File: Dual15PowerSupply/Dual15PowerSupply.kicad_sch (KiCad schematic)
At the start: 40 parts, among them J1 120VAC, J2 +/-15VDC, U1 LT3091xT7, U2 LT3081

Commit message: Design rules for creepage
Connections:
- net Vin-: now reaches C4.2, R1.1, R3.1, U1.3 (~{SHDN}), U1.4 (IN)
- net Vin+: now reaches C3.1, R2.2, U2.6 (IN)
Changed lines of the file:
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@@
+		)
+	)
+	(label "Vin+"
+		(at 140.97 30.48 0)
+		(effects
+			(font
+				(size 1.27 1.27)
+			)
+			(justify left bottom)
 		)
 	)
@@
 		(effects
 			(font
+				(size 1.27 1.27)
+			)
+			(justify left bottom)
+		)
+	)
+	(label "Vin-"
+		(at 140.97 86.36 0)
+		(effects
+			(font

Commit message: Layout in work
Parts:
- U1: value LT3091xT7 -> LT3091
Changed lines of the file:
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@@
 			)
 		)
-		(property "Value" "LT3091xT7"
+		(property "Value" "LT3091"
 			(at 173.99 93.98 0)
 			(show_name no)

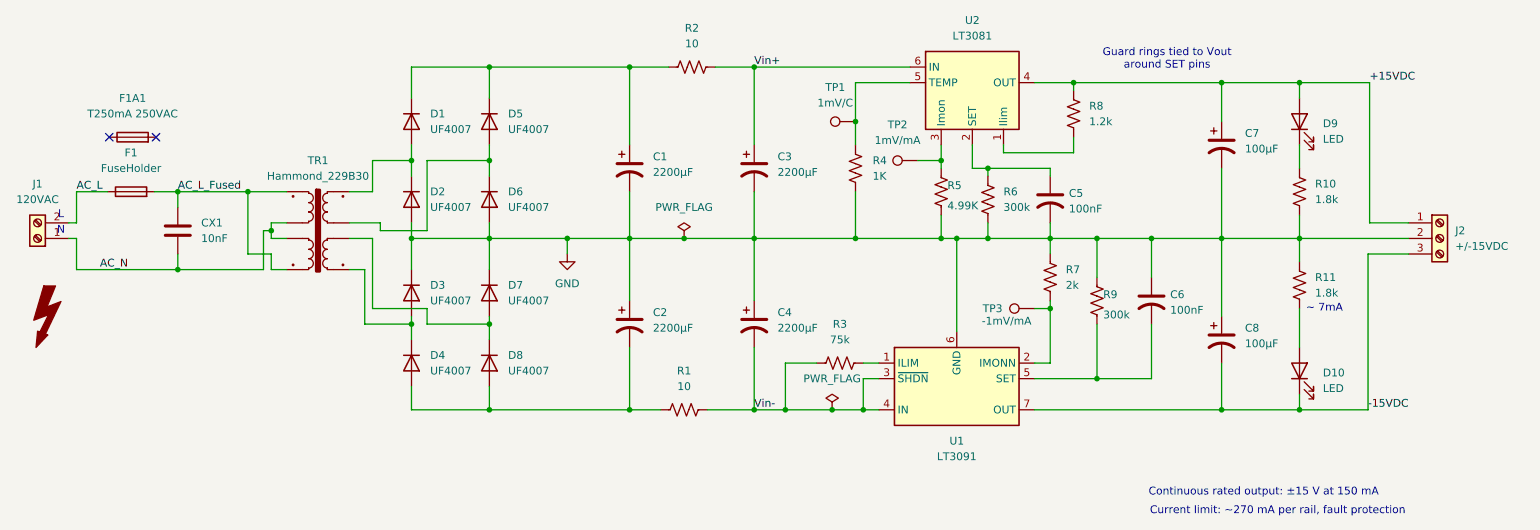
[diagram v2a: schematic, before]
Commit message: Change to SMD bridge rectifiers
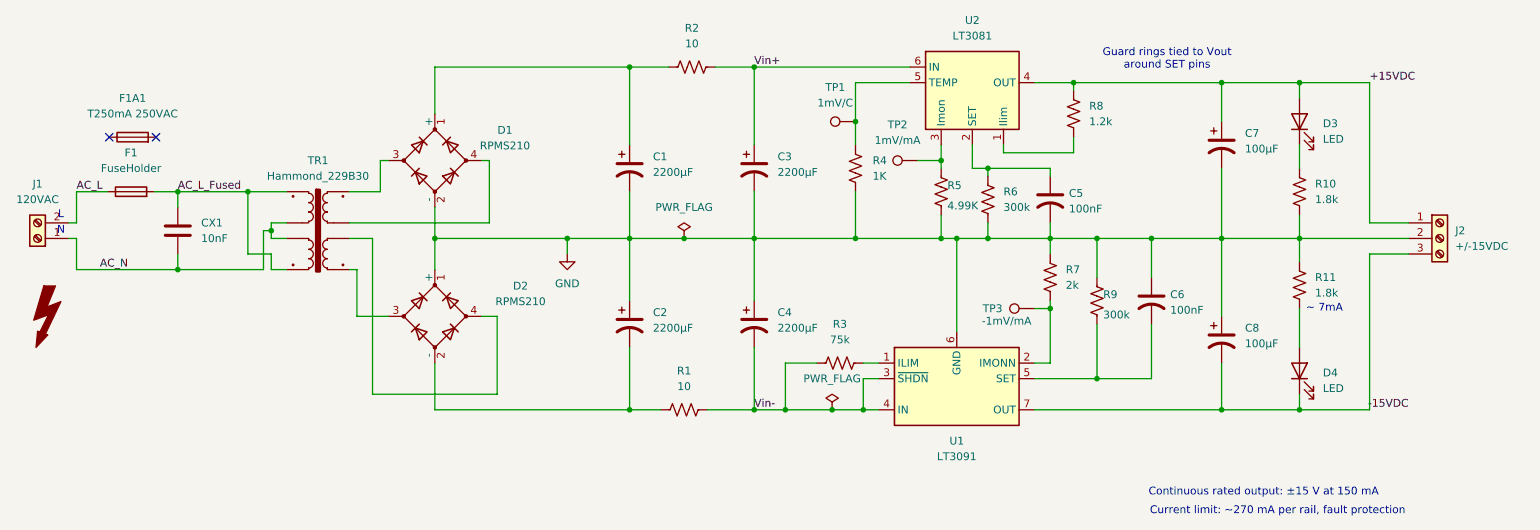
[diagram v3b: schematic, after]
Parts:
- removed D1, D2, D3, D4, D5, D6, D7, D8: UF4007, Diode_THT:D_DO-41_SOD81_P10.16mm_Horizontal, symbol Device:D
- added D1, D2: RPMS210, Diode_SMD_Bridge:Diode_Bridge_Panjit_M4_RPMS210, symbol Device:D_Bridge_+-AA
- R10, R11: footprint Resistor_THT:R_Axial_DIN0207_L6.3mm_D2.5mm_P15.24mm_Horizontal -> Resistor_SMD:R_1206_3216Metric_Pad1.30x1.75mm_HandSolder; MPN MF1/4LCT52R182J -> RT1206FRE071K8L; Mouser 660-MF1/4LCT52R182J -> 603-RT1206FRE071K8L
- TP1, TP2, TP3: MPN (none) -> 5005; Mouser (none) -> 534-5005
- renumbered D9 to D3, D10 to D4
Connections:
- net GND: now also D1.2 (-), D2.1 (+)
- net at C1.1, R2.1: now also D1.1 (+)
- net at TR1.8: now also D1.4
- net at TR1.7: now also D1.3
- net at TR1.5: now also D2.3
- net at TR1.6: now also D2.4
- net at C2.2, R1.2: now also D2.2 (-)

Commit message: Layout in progress
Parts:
- C1, C2: value 2200µF -> 1000µF; footprint Capacitor_THT:CP_Radial_D16.0mm_P7.50mm -> Capacitor_THT:CP_Radial_D12.5mm_P5.00mm; MPN UPW1V222MHD -> EEU-FR1V102; Mouser 647-UPW1V222MHD -> 667-EEU-FR1V102
- C3, C4: footprint Capacitor_THT:CP_Radial_D16.0mm_P7.50mm -> Capacitor_THT:CP_Radial_D12.5mm_P5.00mm; MPN UPW1V222MHD -> EEU-FR1V222L; Mouser 647-UPW1V222MHD -> 667-EEU-FR1V222L
- F1: footprint Fuseholder_Wurth:Wurth_WR-FSH_696105003002 -> Fuseholder_Wurth_WR-FSH:J_Wurth_WR-FSH_696105003002
- J1: footprint TerminalBlock_762:MKDS 5_2-7,62 -> TerminalBlock_Phoenix:PHOENIX_1731721; MPN 1717729 -> 1731721; Mouser 651-1717729 -> 651-1731721
- U1: Mouser 584-LT3091ET7#PBF -> 584-LT3091ET7#PBF
- U2: footprint Package_TO_SOT_THT:TO-220-7_P2.54x5.08mm_StaggerOdd_Lead3.08mm_Vertical -> Package_TO_SOT_THT:TO-220-7_P2.54x3.7mm_StaggerOdd_Lead3.8mm_Vertical
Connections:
- net +15VDC: now also J2.3 (Pin_3); no longer J2.1 (Pin_1)
- net -15VDC: now also J2.1 (Pin_1); no longer J2.3 (Pin_3)
- net AC_L: now also J1.1 (Pin_1); no longer J1.2 (Pin_2)
- net AC_N: now also J1.2 (Pin_2); no longer J1.1 (Pin_1)
- net S4: now reaches D2.3, TR1.5
- net S3: now reaches D2.4, TR1.6
- net S1: now reaches D1.3, TR1.7
- net S2: now reaches D1.4, TR1.8
- net RawDC-: now reaches C2.2, D2.2 (-), R1.2
- net RawDC+: now reaches C1.1, D1.1 (+), R2.1
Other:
- moved on the sheet: J1

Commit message: layout
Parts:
- R4: footprint Resistor_SMD:R_1206_3216Metric_Pad1.30x1.75mm_HandSolder -> Resistor_SMD:R_0805_2012Metric_Pad1.20x1.40mm_HandSolder; MPN RC1206FR-101KL -> RT0805FRE071KL; Mouser 603-RC1206FR-101KL -> 603-RT0805FRE071KL
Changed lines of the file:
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@@
 			)
 		)
-		(property "Footprint" "Resistor_SMD:R_1206_3216Metric_Pad1.30x1.75mm_HandSolder"
+		(property "Footprint" "Resistor_SMD:R_0805_2012Metric_Pad1.20x1.40mm_HandSolder"
 			(at 158.496 47.244 90)
 			(hide yes)
@@
 			)
 		)
-		(property "MPN" "RC1206FR-101KL "
+		(property "MPN" "RT0805FRE071KL"
 			(at 157.48 46.99 0)
 			(hide yes)
@@
 			)
 		)
-		(property "Mouser" "603-RC1206FR-101KL "
+		(property "Mouser" "603-RT0805FRE071KL "
 			(at 157.48 46.99 0)
 			(hide yes)

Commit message: in work
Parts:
- R5: footprint Resistor_SMD:R_1206_3216Metric_Pad1.30x1.75mm_HandSolder -> Resistor_SMD:R_0805_2012Metric_Pad1.20x1.40mm_HandSolder; MPN RC1206FR-074K99L -> RT0805FRD074K99L; Mouser 603-RC1206FR-074K99L -> 603-RT0805FRD074K99L
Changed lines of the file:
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@@
 			)
 		)
-		(property "Footprint" "Resistor_SMD:R_1206_3216Metric_Pad1.30x1.75mm_HandSolder"
+		(property "Footprint" "Resistor_SMD:R_0805_2012Metric_Pad1.20x1.40mm_HandSolder"
 			(at 172.466 51.054 90)
 			(hide yes)
@@
 			)
 		)
-		(property "Datasheet" ""
+		(property "Datasheet" "https://www.mouser.com/datasheet/3/72/1/PYU_RT_1_TO_0_01_ROHS_L.pdf"
 			(at 171.45 50.8 0)
 			(hide yes)
@@
 			)
 		)
-		(property "Description" "Resistor, US symbol"
+		(property "Description" "Resistor, 0805 4.99k.  1% 25ppm  (over spec'd but inexpensive part)"
 			(at 171.45 50.8 0)
 			(hide yes)
@@
 			)
 		)
-		(property "MPN" "RC1206FR-074K99L "
+		(property "MPN" "RT0805FRD074K99L"
 			(at 171.45 50.8 0)
 			(hide yes)
@@
 			)
 		)
-		(property "Mouser" "603-RC1206FR-074K99L "
+		(property "Mouser" "603-RT0805FRD074K99L "
 			(at 171.45 50.8 0)
 			(hide yes)

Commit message: in progress
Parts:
- R3: footprint Resistor_SMD:R_1206_3216Metric_Pad1.30x1.75mm_HandSolder -> Resistor_SMD:R_0805_2012Metric_Pad1.20x1.40mm_HandSolder; MPN RE1206FRE0775KL -> RC0805FR-0775KL; Mouser 603-RE1206FRE0775KL -> 603-RC0805FR-0775KL
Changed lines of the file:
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@@
 			)
 		)
-		(property "Footprint" "Resistor_SMD:R_1206_3216Metric_Pad1.30x1.75mm_HandSolder"
+		(property "Footprint" "Resistor_SMD:R_0805_2012Metric_Pad1.20x1.40mm_HandSolder"
 			(at 155.194 77.724 90)
 			(hide yes)
@@
 			)
 		)
-		(property "Datasheet" "https://www.mouser.com/datasheet/3/508/1/pyu-re_105_rohs_l.pdf"
+		(property "Datasheet" "https://www.mouser.com/catalog/specsheets/YAGEO_PYu_RC_Group_51_RoHS_L_12.pdf"
 			(at 154.94 78.74 0)
 			(hide yes)
@@
 			)
 		)
-		(property "Description" "Resistor,75k 1% 100ppm, 0805 or 1206. Selected part is 50ppm 1206 - revisit if layout needs smaller part."
+		(property "Description" "Resistor,75k 1% 100ppm, 0805"
 			(at 154.94 78.74 0)
 			(hide yes)
@@
 			)
 		)
-		(property "MPN" "RE1206FRE0775KL"
+		(property "MPN" "RC0805FR-0775KL "
 			(at 154.94 78.74 90)
 			(hide yes)
@@
 			)
 		)
-		(property "Mouser" "603-RE1206FRE0775KL "
+		(property "Mouser" "603-RC0805FR-0775KL "
 			(at 154.94 78.74 90)
 			(hide yes)
